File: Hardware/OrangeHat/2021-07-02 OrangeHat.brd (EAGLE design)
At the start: 84.8 x 55.9 mm, 46 parts, among them CON485A JACK_SMD_3MM5, CON485B JACK_SMD_3MM5, IC485 SN75176

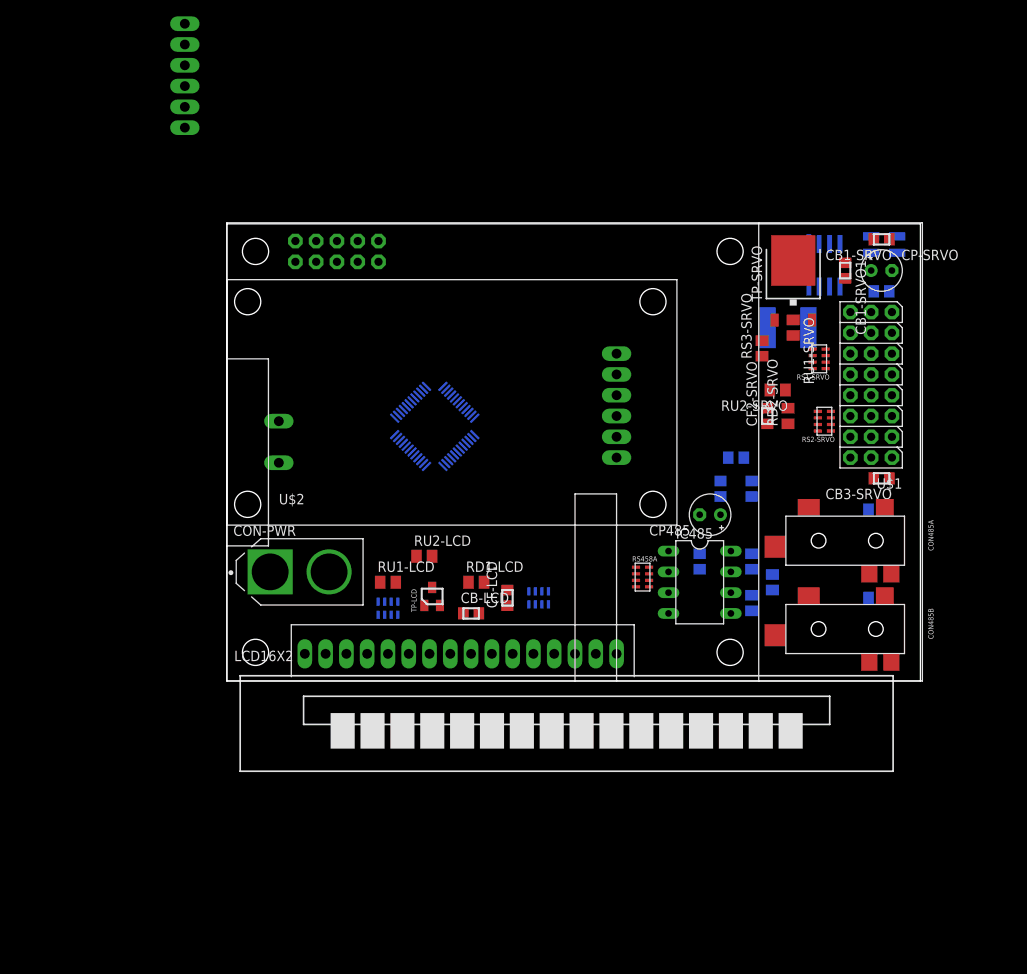
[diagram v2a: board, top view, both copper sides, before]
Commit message: Add files via upload
Adds LED for servo power
Tidy up packages and keepouts
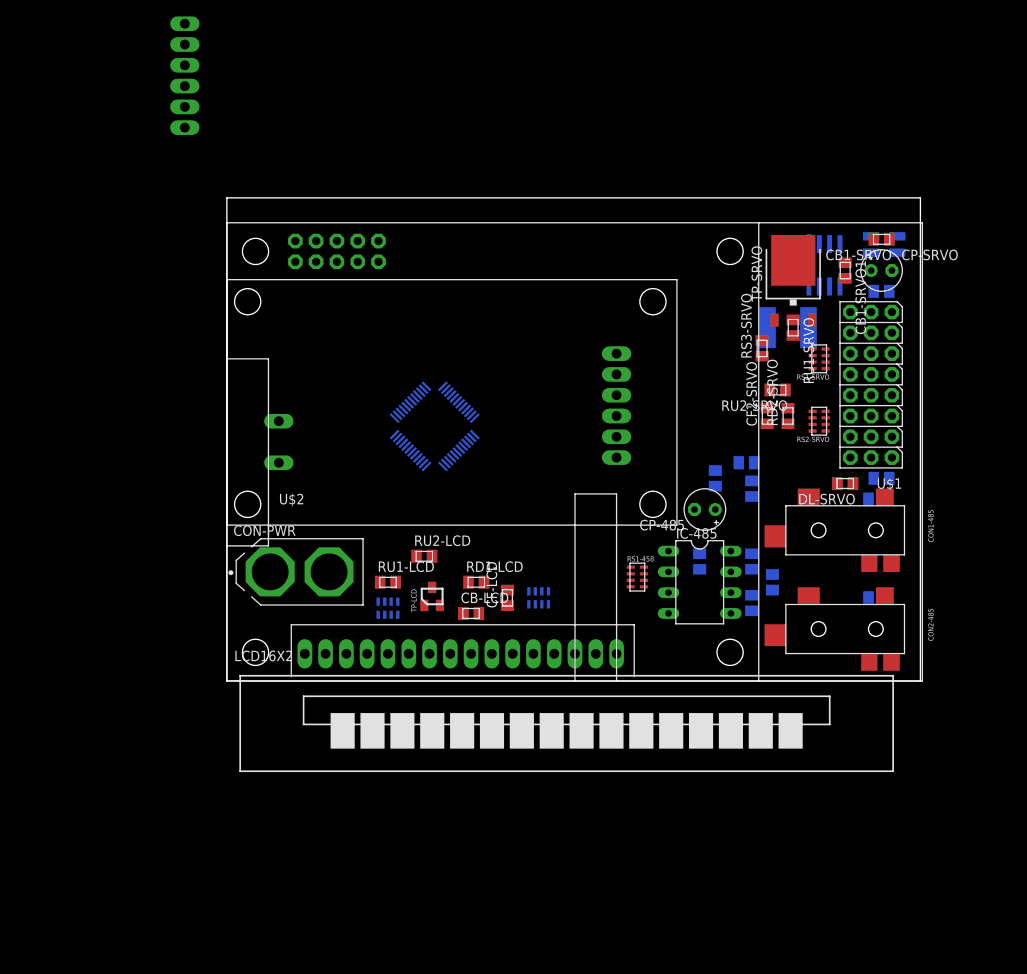
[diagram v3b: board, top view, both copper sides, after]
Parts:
- removed CB485: 100n 50V, 2021-07-02 OrangeHat Library:C0805
- removed CF485: 100n 50v, 2021-07-02 OrangeHat Library:C0805
- removed CON485A: JACK_SMD_3MM5, 2021-07-02 OrangeHat Library:JACK_SMD_3MM5
- removed CP485: 100uF 6V3, 2021-07-02 OrangeHat Library:E2,5-5
- removed LF485A, LF485B: BEAD 500mA, 2021-07-02 OrangeHat Library:C0805
- removed RPD485, RPU485: 720, 2021-07-02 OrangeHat Library:M0805
- removed RS458A: 4X 1K, 2021-07-02 OrangeHat Library:RAC1206
- removed RS485B, RS485C: 10, 2021-07-02 OrangeHat Library:R0805
- removed RT485: 120, 2021-07-02 OrangeHat Library:M0805
- added CB-485: 100n 50V, 2021-07-02 OrangeHat Library:SMD-M2012
- added CF-485: 100n 50v, 2021-07-02 OrangeHat Library:SMD-M2012
- added CON1-485: JACK_SMD_3MM5, 2021-07-02 OrangeHat Library:JACK_SMD_3MM5
- added CP-485: 100uF 6V3, 2021-07-02 OrangeHat Library:E2,5-5
- added DL-SRVO: LED, 2021-07-02 OrangeHat Library:SMD-M2012-POL
- added LF1-485, LF2-485: BEAD 500mA, 2021-07-02 OrangeHat Library:SMD-M2012
- added RD-485, RU-485: 720, 2021-07-02 OrangeHat Library:SMD-M2012
- added RD-SRVO: 1K, 2021-07-02 OrangeHat Library:SMD-M2012
- added RS1-458: 4X 1K, 2021-07-02 OrangeHat Library:RAC1206
- added RS2-485, RS3-485: 10, 2021-07-02 OrangeHat Library:SMD-M2012
- added RT-485: 120, 2021-07-02 OrangeHat Library:SMD-M2012
- CB-LCD, CB1-SRVO, CB1-SRVO1, CB2-SRVO, CB3-SRVO, CF-LCD, CF2-SRVO: device 2021-07-02 OrangeHat Library:C0805 -> 2021-07-02 OrangeHat Library:SMD-M2012
- RD1-LCD, RD2-SRVO, RS3-SRVO, RU1-LCD, RU1-SRVO, RU2-LCD, RU2-SRVO: device 2021-07-02 OrangeHat Library:M0805 -> 2021-07-02 OrangeHat Library:SMD-M2012
- moved RS2-SRVO 0.64 mm to (72.4, 31.8)
- flipped CB3-SRVO to the bottom, turned to 0 degrees
- renumbered CON485B to CON2-485, IC485 to IC-485, U$3 to IC-SRVO
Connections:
- new net N$22: DL-SRVO.+, RD-SRVO.2
- net CHA485: now also CON1-485.L, CON1-485.LX, RD-485.2, RT-485.1; no longer CON485A.L, CON485A.LX, RPD485.2, RT485.1
- net CHB485: now also CON1-485.R, CON1-485.RX, RT-485.2, RU-485.1; no longer CON485A.R, CON485A.RX, RPU485.1, RT485.2
- net N$1: now also RS1-458.1B; no longer RS458A.1B
- net N$16: now also RS1-458.4B; no longer RS458A.4B
- net N$17: now also CON1-485.SHIELD, RS2-485.2; no longer CON485A.SHIELD, RS485B.2
- net N$18: now also RS3-485.2; no longer RS485C.2
- net N$19: now also CF-485.1, LF2-485.1; no longer CF485.1, LF485B.1
- net N$2: now also RS1-458.2B; no longer RS458A.2B
- net N$20: now also CF-485.2, LF1-485.1; no longer CF485.2, LF485A.1
- net N$4: now also RS1-458.3B; no longer RS458A.3B
- net UC_RXI485: now also RS1-458.1A; no longer RS458A.1A
- net UC_TXEN485: now also RS1-458.3A; no longer RS458A.3A
- net UC_TXO485: now also RS1-458.4A; no longer RS458A.4A
- net V+485: now also CB-485.2, CP-485.+, LF1-485.2, RU-485.2; no longer CB485.2, CP485.+, LF485A.2, RPU485.2
- net V-485: now also CB-485.1, CP-485.-, LF2-485.2, RD-485.1, RS1-458.2A, RS2-485.1, RS3-485.1; no longer CB485.1, CP485.-, LF485B.2, RPD485.1, RS458A.2A, RS485B.1, RS485C.1
- net VSRVO+: now also RD-SRVO.1
- net VSRVO-: now also DL-SRVO.-
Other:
- board size 84.8 x 55.9 mm -> 84.8 x 59 mm

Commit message: Assigns microcontroller pins. Draws power planes.
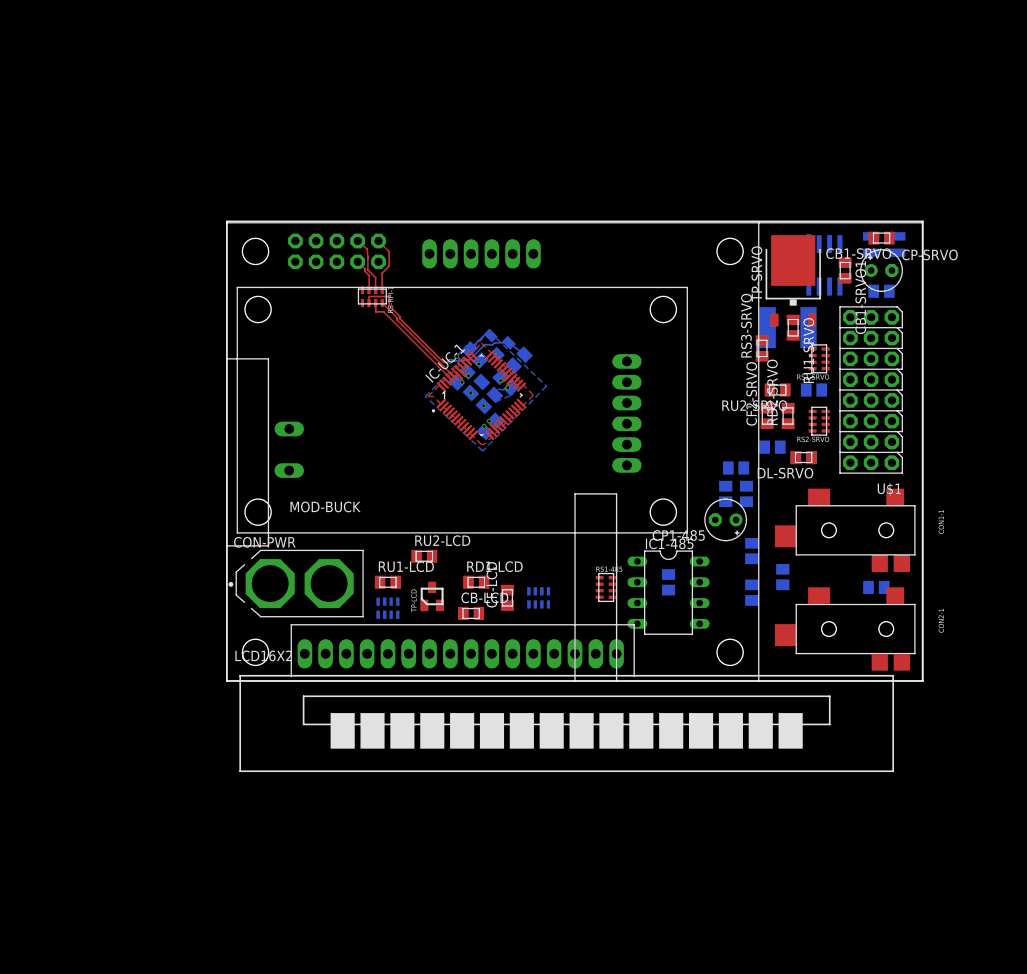
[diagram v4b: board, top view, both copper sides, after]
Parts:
- removed CB-485: 100n 50V, 2021-07-02 OrangeHat Library:SMD-M2012
- removed CF-485: 100n 50v, 2021-07-02 OrangeHat Library:SMD-M2012
- removed CON1-485, CON2-485: JACK_SMD_3MM5, 2021-07-02 OrangeHat Library:JACK_SMD_3MM5
- removed CP-485: 100uF 6V3, 2021-07-02 OrangeHat Library:E2,5-5
- removed IC-485: SN75176, 2021-07-02 OrangeHat Library:DIL08
- removed LF1-485, LF2-485: BEAD 500mA, 2021-07-02 OrangeHat Library:SMD-M2012
- removed RS1-458: 4X 1K, 2021-07-02 OrangeHat Library:RAC1206
- removed U$2: 2020-03-18-BUCK, 2021-07-02 OrangeHat Library:2020-03-18-BUCK
- removed UC1: ATMEGA4809-AFR, 2021-07-02 OrangeHat Library:QFP50P900X900X120-48N
- added CB-UC-1, CB-UC-2, CB-UC-3, CB-UC-4, CB1-485: 100n 50V, 2021-07-02 OrangeHat Library:SMD-M2012
- added CF1-485: 100n 50v, 2021-07-02 OrangeHat Library:SMD-M2012
- added CON1-1, CON2-1: JACK_SMD_3MM5, 2021-07-02 OrangeHat Library:JACK_SMD_3MM5
- added CP1-485: 100uF 6V3, 2021-07-02 OrangeHat Library:E2,5-5
- added IC-UC-1: ATMEGA4809-AFR, 2021-07-02 OrangeHat Library:QFP50P900X900X120-48N
- added IC1-485: SN75176, 2021-07-02 OrangeHat Library:DIL08
- added LF-UC-1, LF1-1, LF2-1: BEAD 500mA, 2021-07-02 OrangeHat Library:SMD-M2012
- added MOD-BUCK: 2020-03-18-BUCK, 2021-07-02 OrangeHat Library:2020-03-18-BUCK
- added RD-UC-1, RU-UC-1: 100k, 2021-07-02 OrangeHat Library:SMD-M2012
- added RS-RPI-1, RS1-485: 4X 1K, 2021-07-02 OrangeHat Library:RAC1206
- added TN-UC-1: MOS-N-SOT23, 2021-07-02 OrangeHat Library:SOT23
- moved IMU1 41.9 mm to (23.2, 24.2), turned to 90 degrees
- moved CB3-SRVO 13.6 mm to (71.8, 35.6)
- moved RS2-485 10.2 mm to (70.5, 27.3)
- moved RD-SRVO 9.94 mm to (66.7, 28.6)
- moved DL-SRVO 5.99 mm to (70.5, 27.3)
- moved CON-PWR 1.43 mm to (8.89, 11.9)
- moved RT-485 1.42 mm to (67.9, 12.7)
- moved RD-485 1.27 mm to (64.1, 10.8)
- moved RS3-485 1.27 mm to (79.4, 11.4)
- moved RU-485 1.27 mm to (64.1, 15.9)
- moved U$1 0.63 mm to (81.3, 44.5)
- moved CB1-SRVO 0.16 mm to (80.0, 54.1)
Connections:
- removed net AVDD: UC1.28
- removed net GND: UC1.15, UC1.29, UC1.43
- removed net IMU-SCL: IMU1.SCL
- removed net IMU-SDA: IMU1.SDA
- removed net N$1: IC-485.1, RS1-458.1B
- removed net N$16: IC-485.4, RS1-458.4B
- removed net N$18: CON2-485.SHIELD, RS3-485.2
- removed net N$2: IC-485.2, RS1-458.2B
- removed net N$4: IC-485.3, RS1-458.3B
- removed net RPI-COM: CON-RPI.6, CON-RPI.9
- removed net RPI-VCC: CON-RPI.2, CON-RPI.4
- removed net UC_RXI485: RS1-458.1A
- removed net UC_TXEN485: RS1-458.3A
- removed net UC_TXO485: RS1-458.4A
- removed net V5.0A1.0+: U$2.V5.0+
- removed net V5.0A1.0-: U$2.V5.0-
- removed net V5.2A3.0+: U$2.V5.2+
- removed net V5.2A3.0-: U$2.V5.2-
- removed net V5.8A3.0+: U$2.V5.8+
- removed net V5.8A3.0-: U$2.V5.8-
- removed net VDD: UC1.14, UC1.42
- new net N$14: IC-UC-1.38
- new net N$42: IC-UC-1.26
- new net N$43: IC-UC-1.25
- new net N$44: IC1-485.3, RS1-485.3B
- new net N$45: IC1-485.4, RS1-485.4B
- new net N$46: CON1-1.SHIELD, RS2-485.2
- new net N$47: CON2-1.SHIELD, RS3-485.2
- new net N$49: IC-UC-1.19
- new net N$50: IC-UC-1.18
- new net N$51: IC-UC-1.17
- new net N$52: IC-UC-1.16
- new net N$53: RS-RPI-1.4B
- new net N$62: IC-UC-1.2
- new net N$8: IC-UC-1.39
- new net UC-485-RXEN#: IC-UC-1.13, RS1-485.2A
- new net UC-485-RXI: IC-UC-1.11, RS1-485.1A
- new net UC-485-TXEN: IC-UC-1.12, RS1-485.3A
- new net UC-485-TXO: IC-UC-1.10, RS1-485.4A
- new net UC-IMU-FSYNC: IC-UC-1.1, IMU1.FSYNC
- new net UC-IMU-INT: IC-UC-1.48, IMU1.INT
- new net UC-IMU-SCL: IC-UC-1.47, IMU1.SCL
- new net UC-IMU-SDA: IC-UC-1.46, IMU1.SDA
- new net UC-IRPI: IC-UC-1.22
- new net UC-RPI-RXI: IC-UC-1.45, RS-RPI-1.2B
- new net UC-RPI-TXO: IC-UC-1.44, RS-RPI-1.1B
- new net UC-RST#: IC-UC-1.40, RU-UC-1.1, TN-UC-1.3
- new net UC-VIN: IC-UC-1.20
- new net UC-VRPI: IC-UC-1.21
- new net VADC+: CB-UC-4.2, IC-UC-1.28, LF-UC-1.2
- new net VRPI+: CON-RPI.2, CON-RPI.4, MOD-BUCK.V5.2+
- new net VRPI-: CON-RPI.6, CON-RPI.9, MOD-BUCK.V5.2-
- net CHA485: now also CON1-1.L, CON1-1.LX, CON2-1.L, CON2-1.LX, IC1-485.6; no longer CON1-485.L, CON1-485.LX, CON2-485.L, CON2-485.LX, IC-485.6
- net CHB485: now also CON1-1.R, CON1-1.RX, CON2-1.R, CON2-1.RX, IC1-485.7; no longer CON1-485.R, CON1-485.RX, CON2-485.R, CON2-485.RX, IC-485.7
- net N$17: now also RS-RPI-1.4A; no longer CON1-485.SHIELD, RS2-485.2
- net N$19: now also CF1-485.1, IC1-485.1, LF2-1.1, RS1-485.1B; no longer CF-485.1, LF2-485.1
- net N$20: now also CF1-485.2, IC1-485.2, LF1-1.1, RS1-485.2B; no longer CF-485.2, LF1-485.1
- net RPI-RST: now also RS-RPI-1.3A
- net RPI-RXI: now also RS-RPI-1.1A
- net RPI-TXO: now also RS-RPI-1.2A
- net UC-ISRVO: now also IC-UC-1.24
- net UC-LCD-D4: now also IC-UC-1.4
- net UC-LCD-D5: now also IC-UC-1.5
- net UC-LCD-D6: now also IC-UC-1.6
- net UC-LCD-D7: now also IC-UC-1.7
- net UC-LCD-EN: now also IC-UC-1.8
- net UC-LCD-PWR#: now also IC-UC-1.3
- net UC-LCD-RS: now also IC-UC-1.9
- net UC-RST: now also RD-UC-1.2, RS-RPI-1.3B, TN-UC-1.1; no longer UC1.40
- net UC-SRVO-PWR#: now also IC-UC-1.27
- net UC-SRVO1: now also IC-UC-1.30
- net UC-SRVO2: now also IC-UC-1.31
- net UC-SRVO3: now also IC-UC-1.32
- net UC-SRVO4: now also IC-UC-1.33
- net UC-SRVO5: now also IC-UC-1.34
- net UC-SRVO6: now also IC-UC-1.35
- net UC-SRVO7: now also IC-UC-1.36
- net UC-SRVO8: now also IC-UC-1.37
- net UC-UPDI: now also IC-UC-1.41; no longer UC1.41
- net UC-VSRVO: now also IC-UC-1.23
- net V+485: now also CB1-485.2, CP1-485.+, IC1-485.8, LF1-1.2; no longer CB-485.2, CP-485.+, IC-485.8, LF1-485.2
- net V-485: now also CB1-485.1, CP1-485.-, IC1-485.5, LF2-1.2; no longer CB-485.1, CP-485.-, IC-485.5, LF2-485.2, RS1-458.2A
- net VIN+: now also MOD-BUCK.VIN+; no longer U$2.VIN+
- net VIN-: now also MOD-BUCK.VIN-; no longer U$2.VIN-
- net VSRVO+: now also MOD-BUCK.V5.8+
- net VSRVO-: now also MOD-BUCK.V5.8-
- net VUC+: now also CB-UC-1.2, CB-UC-2.2, CB-UC-3.2, IC-UC-1.14, IC-UC-1.42, LF-UC-1.1, MOD-BUCK.V5.0+, RU-UC-1.2
- net VUC-: now also CB-UC-1.1, CB-UC-2.1, CB-UC-3.1, CB-UC-4.1, IC-UC-1.15, IC-UC-1.29, IC-UC-1.43, MOD-BUCK.V5.0-, RD-UC-1.1, TN-UC-1.2
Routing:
- net UC-RST: track 0.00 -> 25.4 mm, vias 0 -> 1
- net UC-RPI-RXI: track 0.00 -> 13.5 mm
- net UC-RPI-TXO: track 0.00 -> 12.5 mm
- net RPI-TXO: track 0.00 -> 6.92 mm
- net RPI-RXI: track 0.00 -> 6.86 mm
- net UC-RST#: track 0.00 -> 6.57 mm, vias 0 -> 1
- net VUC-: track 0.00 -> 4.20 mm, vias 0 -> 3
- net RPI-RST: track 0.00 -> 4.02 mm
- net VUC+: track 0.00 -> 3.72 mm, vias 0 -> 5
- net VADC+: track 0.00 -> 1.44 mm, vias 0 -> 1
- added copper zone on layer 16, net VADC+
- added copper zone on layer 1, net VUC+
- added copper zone on layer 16, net VUC-
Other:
- board size 84.8 x 59 mm -> 85.1 x 56.2 mm
